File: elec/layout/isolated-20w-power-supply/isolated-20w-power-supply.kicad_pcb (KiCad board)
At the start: 2 copper layers, 11.3 x 28.3 mm, 10 parts

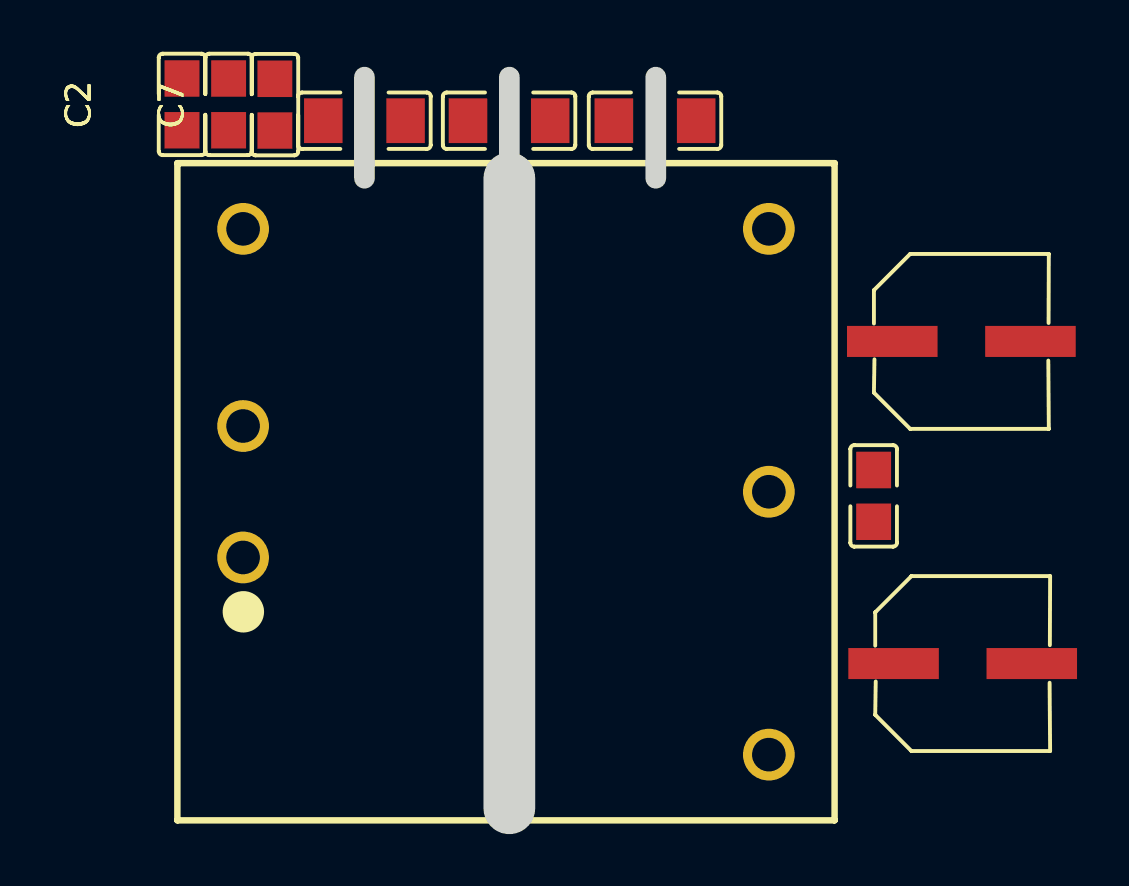
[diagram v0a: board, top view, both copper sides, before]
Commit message: Build everything with ordered params to fix frozen builds
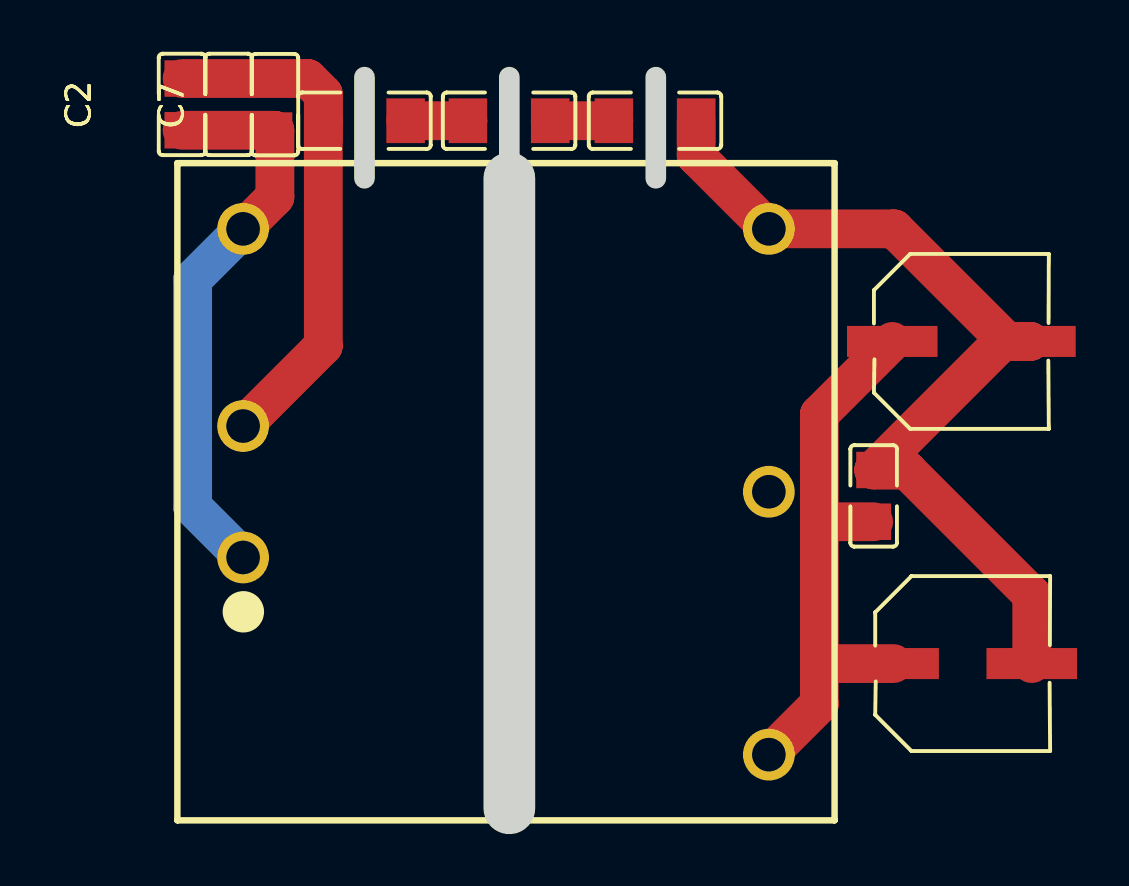
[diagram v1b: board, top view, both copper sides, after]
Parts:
- C5, C6, C9: value 2.2nF ±5% 1kV C0G -> 2.2nF ±10% 1kV X7R
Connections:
- C1 pad 2: gnd-1 -> gnd
- C2 pad 2: gnd-1 -> gnd
- C3 pad 2: gnd -> gnd-1
- C4 pad 2: gnd -> gnd-1
- C5 pad 1: gnd-1 -> gnd
- C7 pad 2: gnd-1 -> gnd
- C8 pad 2: gnd -> gnd-1
- C9 pad 2: gnd -> gnd-1
- U1 pad 2: gnd-1 -> gnd
- U1 pad 4: gnd -> gnd-1
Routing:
- net gnd-1: track 0.00 -> 36.1 mm
- net hv: track 0.00 -> 23.0 mm
- net hv-1: track 0.00 -> 22.2 mm
- net gnd: track 0.00 -> 19.8 mm
- net net: track 0.00 -> 2.46 mm
- net net-1: track 0.00 -> 2.41 mm

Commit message: checkin
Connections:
- C1 pad 1: hv-1 -> hv
- C2 pad 1: hv-1 -> hv
- C3 pad 1: hv -> hv-1
- C4 pad 1: hv -> hv-1
- C5 pad 2: net-1 -> net
- C6 pad 1: net-1 -> net
- C6 pad 2: net -> net-1
- C7 pad 1: hv-1 -> hv
- C8 pad 1: hv -> hv-1
- C9 pad 1: net -> net-1
- U1 pad 1: hv-1 -> hv
- U1 pad 3: hv-1 -> hv
- U1 pad 6: hv -> hv-1
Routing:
- net hv-1: track 22.2 -> 23.0 mm
- net hv: track 23.0 -> 22.2 mm
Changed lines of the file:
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@@
     (net 0 "")
     (net 1 "NP")
-    (net 2 "net-1")
-    (net 3 "hv")
-    (net 4 "net")
+    (net 2 "net")
+    (net 3 "hv-1")
+    (net 4 "net-1")
     (net 5 "gnd-1")
     (net 6 "gnd")
-    (net 7 "hv-1")
+    (net 7 "hv")
     (footprint "atopile:PWRM-TH_TDPOWER_TDK20-XXSXXWH-ae86e0"
         (layer "F.Cu")
@@
             (drill 1.300023)
             (layers "*.Cu" "*.Mask")
-            (net 7 "hv-1")
+            (net 7 "hv")
             (remove_unused_layers no)
         )
@@
             (drill 1.300023)
             (layers "*.Cu" "*.Mask")
-            (net 7 "hv-1")
+            (net 7 "hv")
             (remove_unused_layers no)
         )
@@
             (drill 1.300023)
             (layers "*.Cu" "*.Mask")
-            (net 3 "hv")
+            (net 3 "hv-1")
             (remove_unused_layers no)
         )
@@
             (size 1.41 1.35)
             (layers "F.Cu" "F.Mask" "F.Paste")
-            (net 7 "hv-1")
+            (net 7 "hv")
         )
         (pad "2" smd rect
@@
             (size 1.41 1.35)
             (layers "F.Cu" "F.Mask" "F.Paste")
-            (net 7 "hv-1")
+            (net 7 "hv")
         )
         (pad "2" smd rect
@@
             (size 3.5 1.2)
             (layers "F.Cu" "F.Mask" "F.Paste")
-            (net 3 "hv")
+            (net 3 "hv-1")
         )
         (pad "2" smd rect
@@
             (size 1.49 1.73)
             (layers "F.Cu" "F.Mask" "F.Paste")
-            (net 4 "net")
+            (net 4 "net-1")
         )
         (pad "2" smd rect
@@
             (size 1.41 1.35)
             (layers "F.Cu" "F.Mask" "F.Paste")
-            (net 3 "hv")
+            (net 3 "hv-1")
         )
         (pad "2" smd rect
@@
             (size 3.5 1.2)
             (layers "F.Cu" "F.Mask" "F.Paste")
-            (net 3 "hv")
+            (net 3 "hv-1")
         )
         (pad "2" smd rect
@@
             (size 1.41 1.35)
             (layers "F.Cu" "F.Mask" "F.Paste")
-            (net 7 "hv-1")
+            (net 7 "hv")
         )
         (pad "2" smd rect
@@
             (size 1.49 1.73)
             (layers "F.Cu" "F.Mask" "F.Paste")
-            (net 2 "net-1")
+            (net 2 "net")
         )
         (pad "2" smd rect
@@
             (size 1.49 1.73)
             (layers "F.Cu" "F.Mask" "F.Paste")
-            (net 4 "net")
+            (net 4 "net-1")
         )
         (embedded_fonts no)
@@
             (size 1.49 1.73)
             (layers "F.Cu" "F.Mask" "F.Paste")
-            (net 2 "net-1")
+            (net 2 "net")
         )
         (embedded_fonts no)
